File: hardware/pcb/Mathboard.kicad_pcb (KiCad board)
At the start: 4 copper layers, 95.6 x 73.6 mm, 95 parts, among them J3 TYPE-C sinking plate, Q1 2N7002VC-, Q2 2N7002VC-, SW1 SW_Push, SW10 SW_Push, SW11 SW_Push, SW12 SW_Push, SW13 SW_Push, SW14 SW_Push, SW15 SW_Push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

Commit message: Minor changes for v1.5
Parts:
- H1: footprint MountingHole:MountingHole_2.7mm_M2.5_Pad_TopOnly -> MountingHole:MountingHole_2.7mm_M2.5_Pad
- moved C27 7.01 mm to (131.4, 98.1)
- moved R11 0.66 mm to (170.8, 101.5), turned to -90 degrees
- moved F1 0.44 mm to (142.1, 52.7)
- moved D19 0.16 mm to (142.1, 53.7)
- moved C17 0.10 mm to (160.9, 111.7)
- moved C20 0.08 mm to (138.1, 54.2)
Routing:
- net ROW2: track 130.8 -> 140.5 mm
- net /Microcontroller/QSPI_CS: track 16.3 -> 15.4 mm, vias 1 -> 0
- net GND: track 50.9 -> 51.2 mm, vias 37 -> 35

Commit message: Version 1.5
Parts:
- removed J3: TYPE-C sinking plate, mathboard:USB_C_Receptacle_XYECONN TYPE-C-F02C-1BBWC1.6
- added J1: TYPE-C sinking plate, mathboard:USB_C_Receptacle_XYECONN TYPE-C-F02C-1BBWC1.6, F.Cu at (139.8, 46.9)
- added REF** (x2): OSHW-Logo2_14.6x12mm_Copper, Symbol:OSHW-Logo2_14.6x12mm_Copper, F.Cu at (112.4, 108.9)
- C2: value 100n -> 10n; footprint Capacitor_SMD:C_0402_1005Metric -> Capacitor_SMD:C_0603_1608Metric
- C20: value 10n -> 4.7u; footprint Capacitor_SMD:C_0603_1608Metric -> Capacitor_SMD:C_0402_1005Metric
- C5: value 4.7u -> 100n
- D17: value DSL14 -> D_Zener; footprint Diode_SMD:D_SOD-123 -> mathboard:DFN1006-2L
- D19: value D_Zener -> DSL14; footprint mathboard:DFN1006-2L -> Diode_SMD:D_SOD-123
- moved C20 9.49 mm to (140.3, 63.4)
- moved D19 8.22 mm to (137.1, 60.2), turned to 90 degrees
- moved D17 8.10 mm to (142.0, 53.8), turned to 0 degrees
- moved C5 7.28 mm to (138.2, 57.1), turned to 90 degrees
- moved D11 6.29 mm to (160.8, 93.6), turned to 180 degrees
- moved D12 4.34 mm to (145.8, 92.0)
- moved C21 3.91 mm to (143.9, 61.9)
- moved C2 2.65 mm to (138.2, 54.5), turned to -90 degrees
- moved C9 2.20 mm to (161.7, 87.4), turned to 180 degrees
- moved D4 1.28 mm to (115.1, 61.2)
- moved D5 1.13 mm to (109.5, 61.2)
- moved D9 0.80 mm to (109.5, 64.1)
- moved C25 0.31 mm to (113.4, 62.8)
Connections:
- net /Microcontroller/USB+ renamed USB+
- net /Microcontroller/USB- renamed USB-
- C2 pad 1: Net-(D17-A) -> Net-(D17-K)
- C20 pad 1: Net-(D19-K) -> +5V
- C21 pad 1: +5V -> +3V3
- C5 pad 1: +3V3 -> Net-(D19-A)
- D17 pad 1: +5V -> Net-(D17-K)
- D19 pad 1: Net-(D19-K) -> +5V
- F1 pad 2: Net-(D19-A) -> Net-(D17-A)
- FB1 pad 1: Net-(D19-K) -> Net-(D17-K)
- FB1 pad 2: Net-(D17-A) -> Net-(D19-A)
- U3 pad 4: /Microcontroller/PORT- -> /PORT-
- U3 pad 5: Net-(D19-K) -> Net-(D17-K)
- U3 pad 6: /Microcontroller/PORT+ -> /PORT+
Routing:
- net /PORT-: track 0.00 -> 5.07 mm, vias 0 -> 2
- net /Microcontroller/PORT-: track 5.07 -> 0.00 mm, vias 2 -> 0
- net /PORT+: track 0.00 -> 4.75 mm
- net /Microcontroller/PORT+: track 4.75 -> 0.00 mm
- net ROW2: track 140.5 -> 135.8 mm
- net ROW3: track 101.4 -> 103.0 mm
- net COL1: track 77.9 -> 76.3 mm
- net ROW1: track 110.1 -> 108.6 mm
- net Net-(D4-A): track 4.72 -> 5.90 mm
- net Net-(D5-A): track 13.2 -> 14.3 mm
- net Net-(D19-A): track 1.00 -> 0.00 mm
- net Net-(D17-A): track 0.24 -> 1.00 mm
- added copper zone on F.Cu, net Net-(D17-K)
- added copper zone on F.Cu, net Net-(D19-A)
- removed copper zone on F.Cu, net Net-(D17-A)
- removed copper zone on F.Cu, net Net-(D19-K)

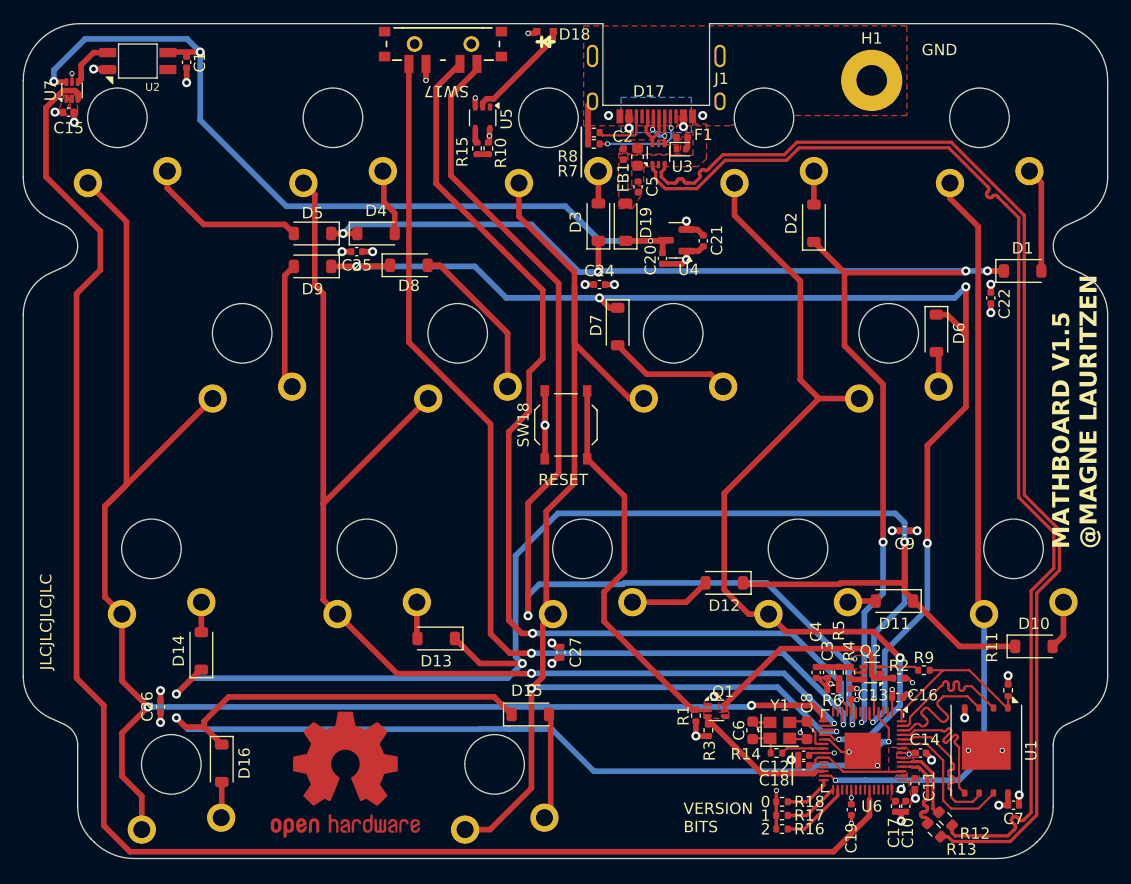
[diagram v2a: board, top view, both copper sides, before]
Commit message: Hotswap sockets and fw improvements
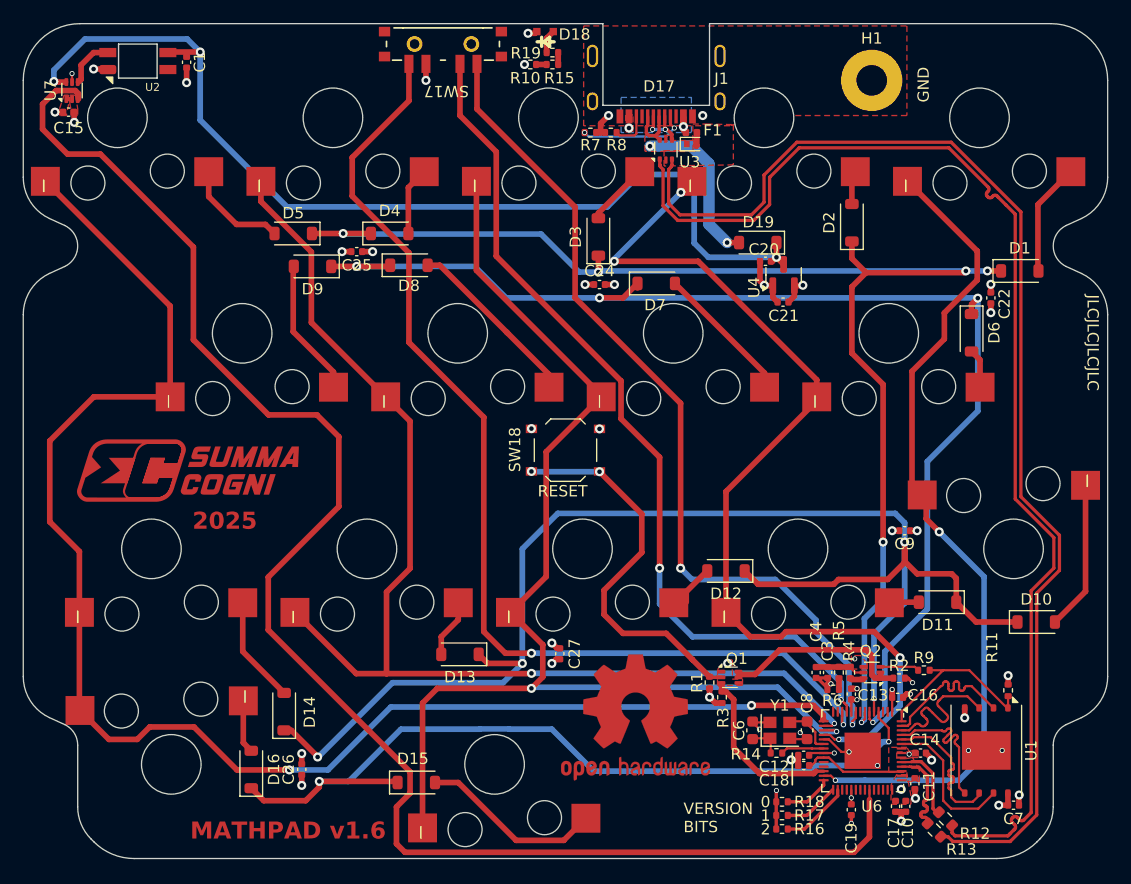
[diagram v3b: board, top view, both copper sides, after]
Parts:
- removed C2: 10n, Capacitor_SMD:C_0603_1608Metric
- removed C5: 100n, Capacitor_SMD:C_0402_1005Metric
- removed FB1: BLM15PX471SN1D, Inductor_SMD:L_0402_1005Metric
- removed U5: PSSI2021SAY, Package_TO_SOT_SMD:SOT-353_SC-70-5
- added R19: 5.1k, Resistor_SMD:R_0402_1005Metric, F.Cu at (130.7, 45.2)
- SW1, SW10, SW11, SW12, SW13, SW14, SW15, SW16, SW2, SW3, SW4, SW5, SW6, SW7, SW8, SW9: value SW_Push -> SW_socket; footprint key-switches:SW_Gateron_LowProfile_THT -> mathboard:SW_Gateron_LowProfile_THT_hotswap
- moved REF** 26.1 mm to (138.0, 103.8) (x2)
- moved C26 13.6 mm to (108.5, 108.5)
- moved D19 11.8 mm to (148.8, 62.0), turned to 180 degrees
- moved D15 11.7 mm to (118.7, 109.6)
- moved U4 9.95 mm to (151.0, 64.9), turned to 90 degrees
- moved R15 9.95 mm to (130.7, 46.3), turned to 180 degrees
- moved C20 9.08 mm to (149.4, 63.6), turned to 180 degrees
- moved D14 9.05 mm to (107.0, 103.3)
- moved C21 8.86 mm to (151.0, 67.2), turned to 180 degrees
- moved R10 8.27 mm to (128.7, 46.3), turned to 180 degrees
- moved D7 5.10 mm to (139.8, 65.6), turned to 0 degrees
- moved D11 3.80 mm to (164.6, 93.7)
- moved D2 3.35 mm to (157.1, 60.2)
- moved R1 3.15 mm to (144.5, 100.8)
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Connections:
- D19 pad 2: Net-(D19-A) -> Net-(D17-K)
- R10 pad 1: +3V3 -> Net-(R10-Pad1)
- R10 pad 2: Net-(R10-Pad2) -> +3V3
- R15 pad 1: Net-(R10-Pad2) -> Net-(R15-Pad1)
- R15 pad 2: Net-(R15-Pad2) -> Net-(R10-Pad1)
- SW10 pad 1: Net-(D10-A) -> COL0
- SW10 pad 2: COL0 -> Net-(D10-A)
- SW16 pad 1: Net-(D16-A) -> COL4
- SW16 pad 2: COL4 -> Net-(D16-A)
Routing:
- net ROW3: track 103.0 -> 72.1 mm
- net /Microcontroller/7: track 94.8 -> 77.5 mm
- net +5V: track 74.3 -> 89.4 mm
- net Net-(D17-K): track 0.00 -> 14.5 mm, vias 0 -> 2
- net /Microcontroller/8: track 89.4 -> 76.5 mm
- net ROW2: track 135.8 -> 124.3 mm
- net COL1: track 76.3 -> 85.5 mm, vias 2 -> 4
- net Net-(D10-A): track 4.29 -> 13.2 mm
- net GND: track 51.0 -> 42.8 mm
- net Net-(D18-K): track 9.60 -> 2.09 mm
- net Net-(D15-A): track 9.39 -> 16.2 mm
- net Net-(D14-A): track 2.65 -> 9.46 mm
- net COL0: track 66.9 -> 73.4 mm, vias 1 -> 2
- net Net-(D5-A): track 14.3 -> 9.35 mm
- net USB+: track 103.0 -> 107.8 mm
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- removed copper zone on F.Cu, net Net-(D19-A)
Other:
- board text added: "2025"
- board text added: "MATHPAD v1.6"
- board text removed: "MATHBOARD V1.5 @MAGNE LAURITZEN"
